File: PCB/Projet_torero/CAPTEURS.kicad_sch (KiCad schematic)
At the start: 0 parts

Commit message: kicad capteurs modif
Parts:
- added C401, C402: C_Small, symbol Device:C_Small
- added U401: ADXL343, Package_LGA:LGA-14_3x5mm_P0.8mm_LayoutBorder1x6y, symbol Sensor_Motion:ADXL343
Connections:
- new net +3.3V: C401.1, U401.3 (RES), U401.6 (Vs)
- new net +3.3VA: C402.1, U401.1 (Vdd_I/O)
- new net CS: U401.7 (~{CS})
- new net GND: C401.2, C402.2, U401.11 (RES), U401.2 (GND), U401.4 (GND), U401.5 (GND)
- new net INT1: U401.8 (INT1)
- new net INT2: U401.9 (INT2)
- new net SCLK: U401.14 (SCL/SCLK)
- new net SDA/SDI/SDIO: U401.13 (SDA/SDI/SDIO)
- new net SDO/ADDR: U401.12 (SDO/ADDR)

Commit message: modif capteurs
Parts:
- added J401: Conn_01x08, symbol Connector_Generic:Conn_01x08
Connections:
- net GND: now also J401.8 (Pin_8)
- new net +5V: J401.5 (Pin_5)
- new net DEV_EN: J401.3 (Pin_3)
- new net M_EN: J401.2 (Pin_2)
- new net M_SCTR: J401.4 (Pin_4)
- new net Rx: J401.7 (Pin_7)
- new net Tx: J401.6 (Pin_6)
- no-connect marks 0 -> 1

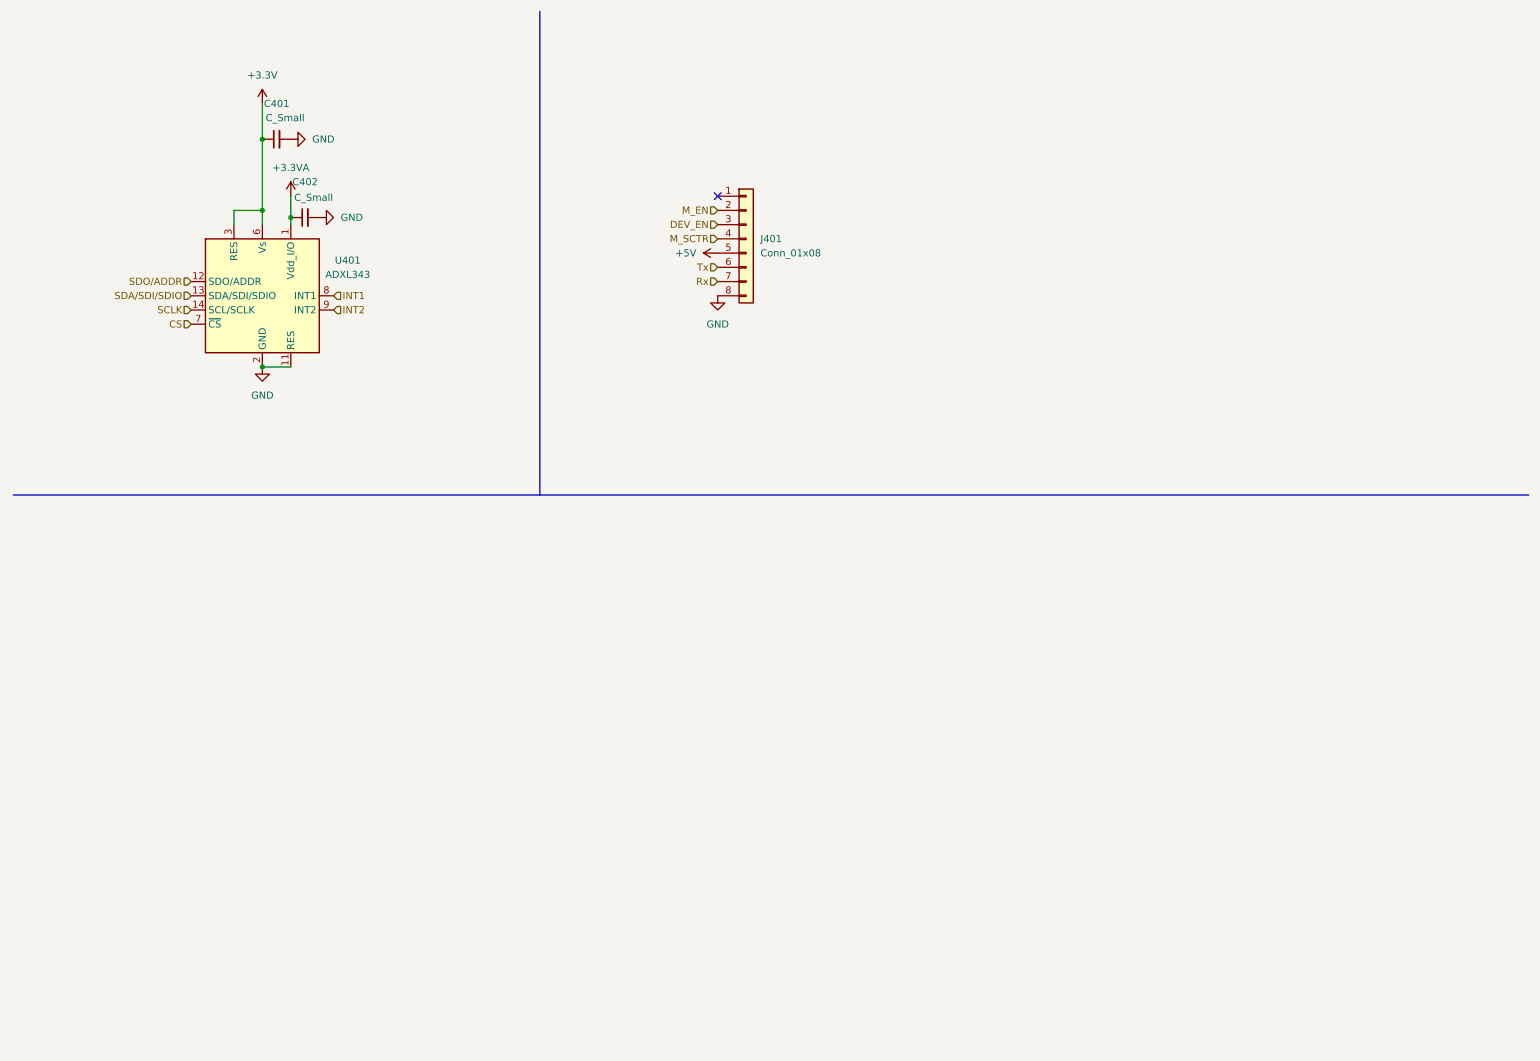
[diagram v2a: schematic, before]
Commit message: modif kicad capteur + excel liens/sources
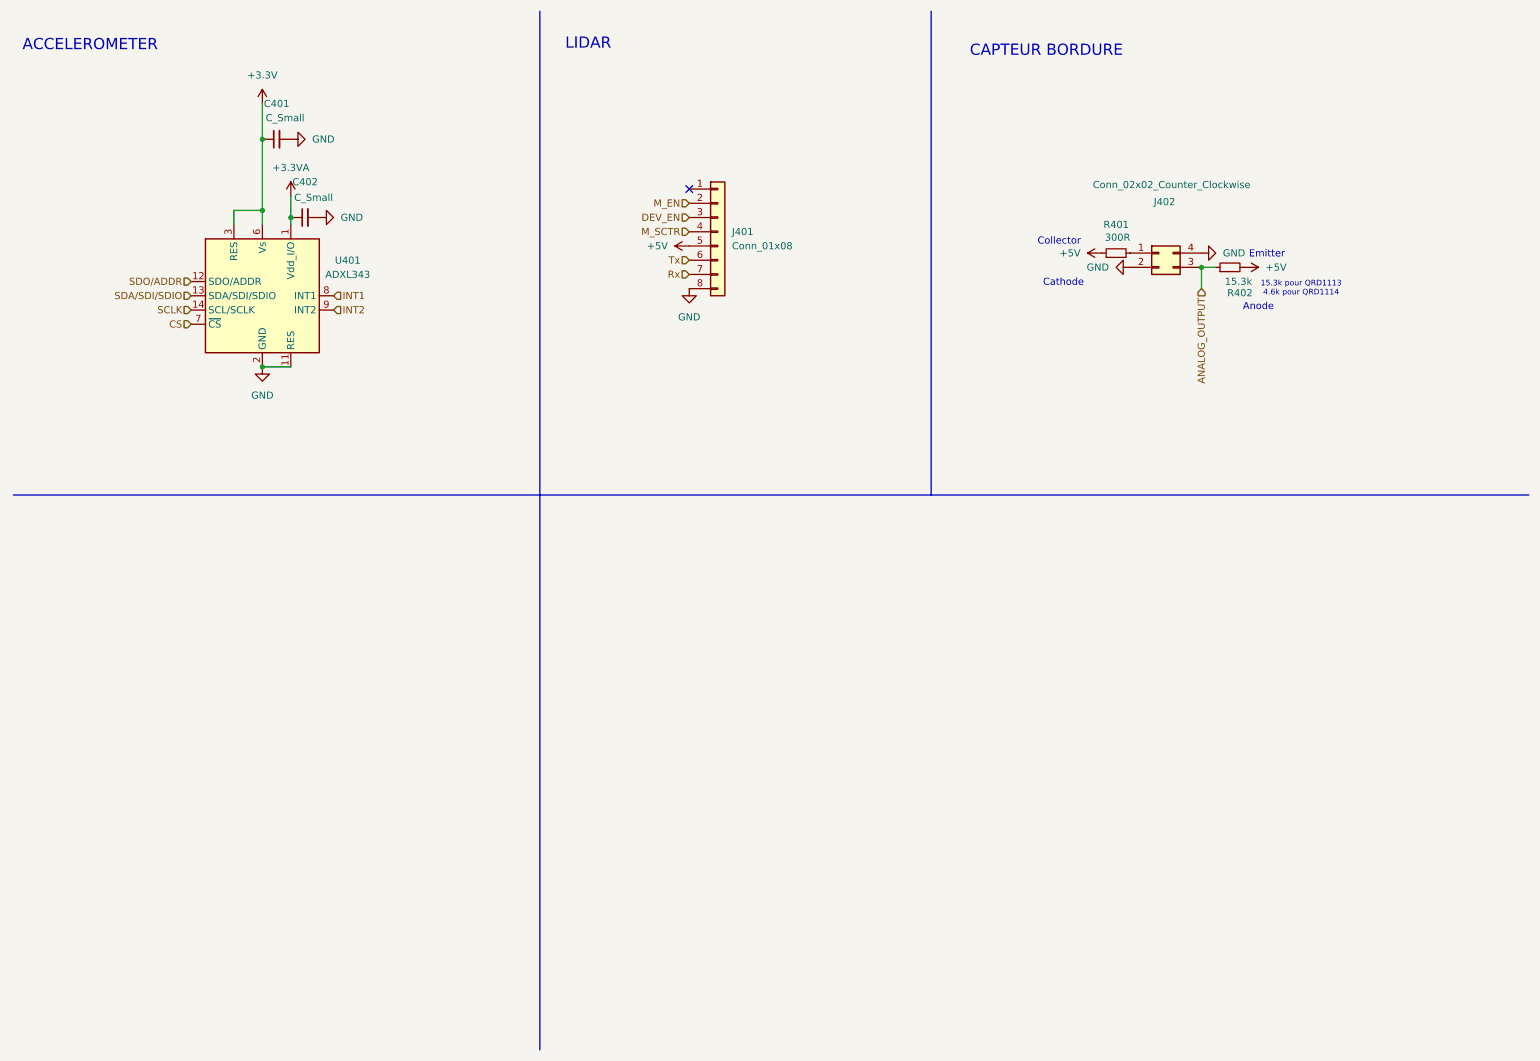
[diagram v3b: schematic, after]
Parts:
- added J402: Conn_02x02_Counter_Clockwise, symbol Connector_Generic:Conn_02x02_Counter_Clockwise
- added R401: 300R, symbol Device:R_Small
- added R402: 15.3k, symbol Device:R_Small
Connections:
- net +5V: now also R401.1, R402.2
- net GND: now also J402.2 (Pin_2), J402.4 (Pin_4)
- new net: J402.1 (Pin_1), R401.2
- new net ANALOG_OUTPUT: J402.3 (Pin_3), R402.1
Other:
- note added: "15.3k pour QRD1113 4.6k pour QRD1114"
- note added: "ACCELEROMETER"
- note added: "Anode"
- note added: "CAPTEUR BORDURE"
- note added: "Cathode"
- note added: "Collector"
- note added: "Emitter"
- note added: "LIDAR"
- moved on the sheet: J401

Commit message: modif kicad capteur
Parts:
- added J403: Conn_02x02_Counter_Clockwise, symbol Connector_Generic:Conn_02x02_Counter_Clockwise
- added R403: 300R, symbol Device:R_Small
- added R404: 15.3k, symbol Device:R_Small
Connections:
- net +5V: now also R403.1, R404.2
- net GND: now also J403.2 (Pin_2), J403.4 (Pin_4)
- net ANALOG_OUTPUT renamed ANALOG_OUTPUT_1
- new net: J403.1 (Pin_1), R403.2
- new net ANALOG_OUTPUT_2: J403.3 (Pin_3), R404.1
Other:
- moved on the sheet: J402, R401, R402

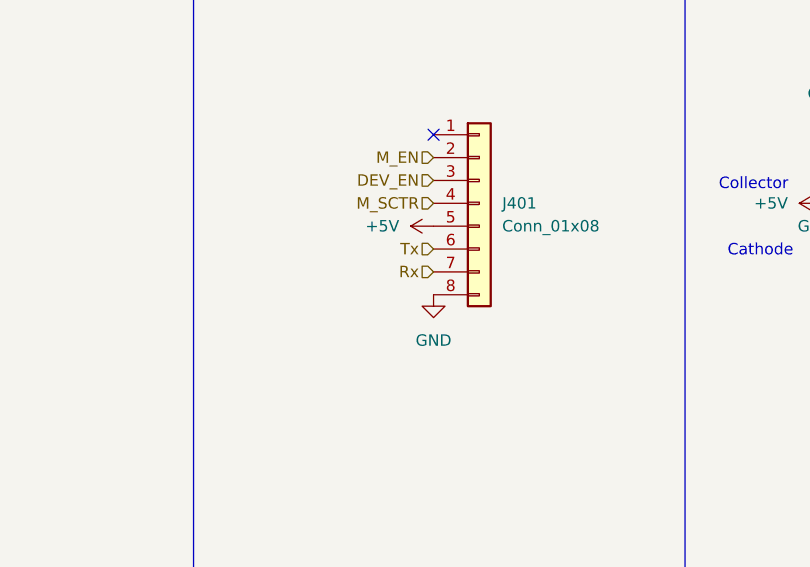
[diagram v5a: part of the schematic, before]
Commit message: Inversion pins lidar
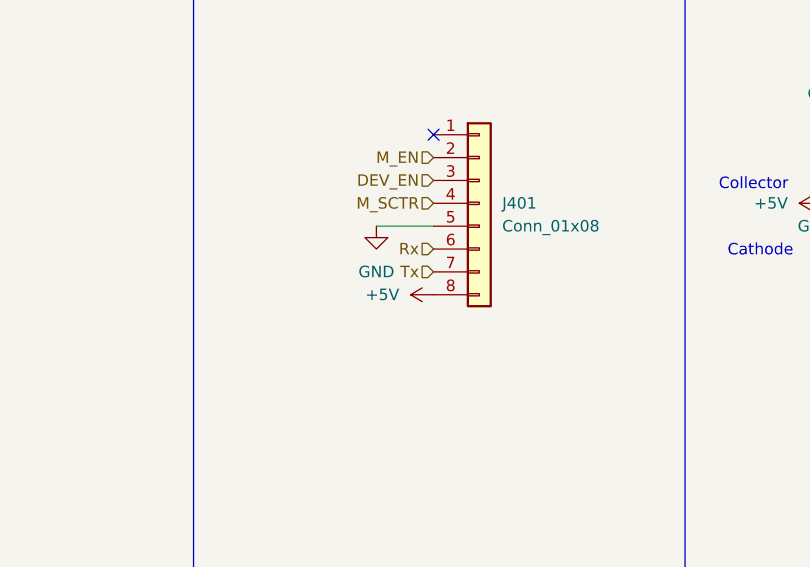
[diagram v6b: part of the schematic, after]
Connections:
- net +5V: now also J401.8 (Pin_8); no longer J401.5 (Pin_5)
- net GND: now also J401.5 (Pin_5); no longer J401.8 (Pin_8)
- net Rx: now also J401.6 (Pin_6); no longer J401.7 (Pin_7)
- net Tx: now also J401.7 (Pin_7); no longer J401.6 (Pin_6)

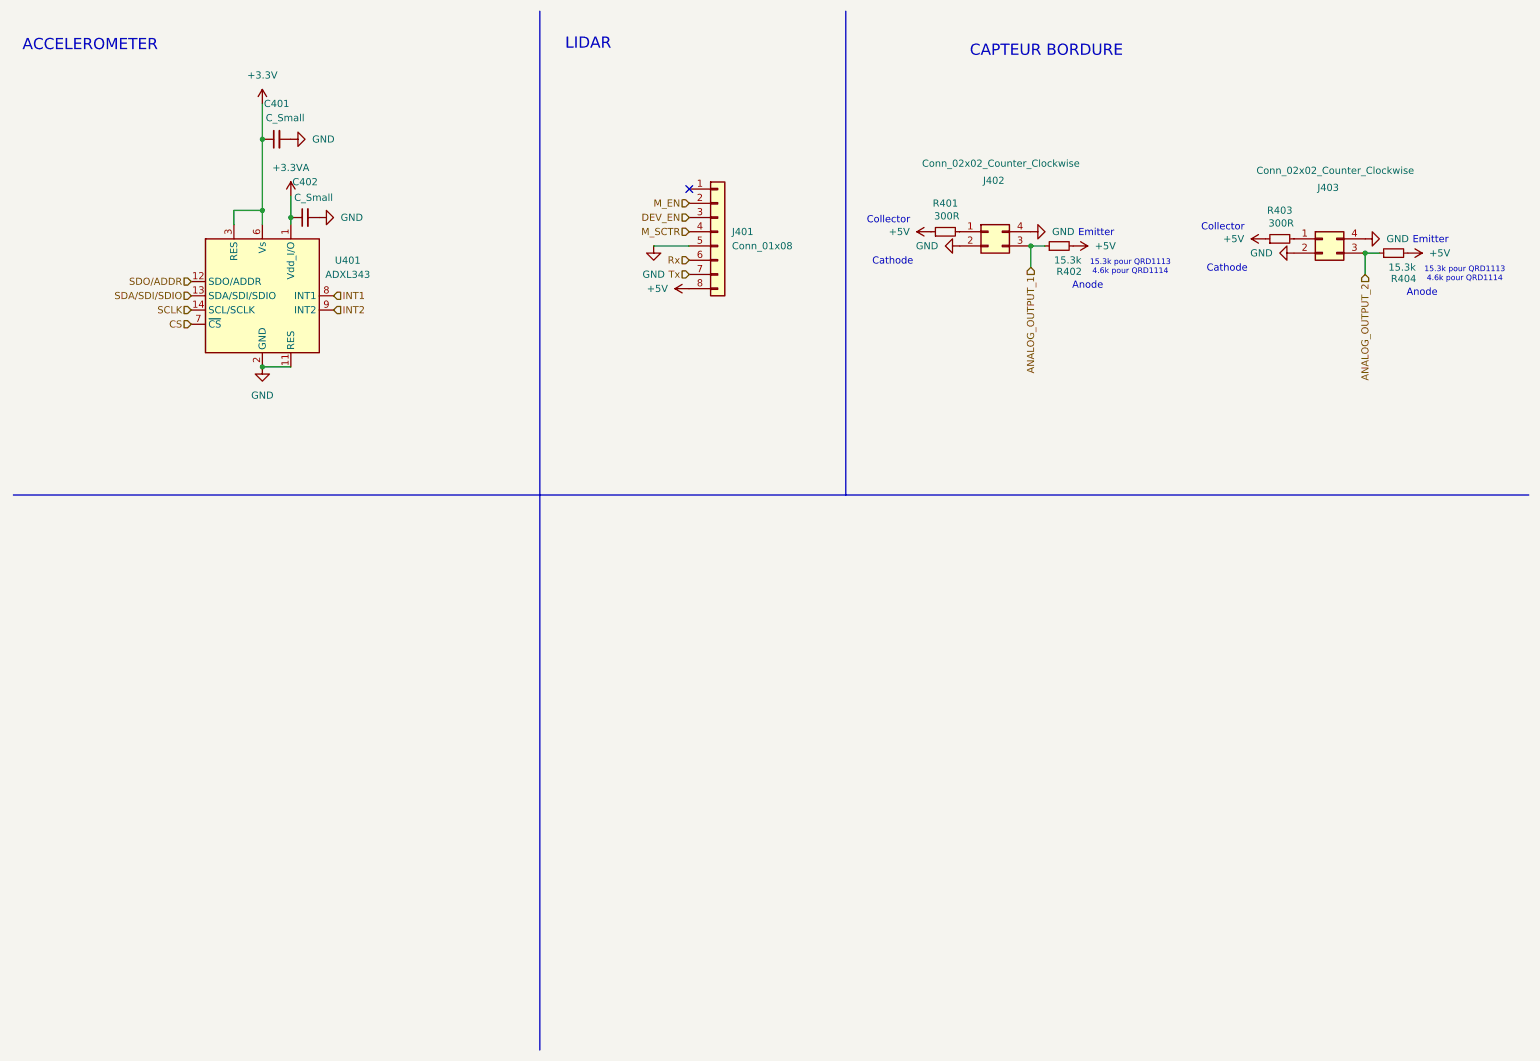
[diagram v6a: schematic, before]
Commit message: ajout nouvelles feuilles capteurs bords
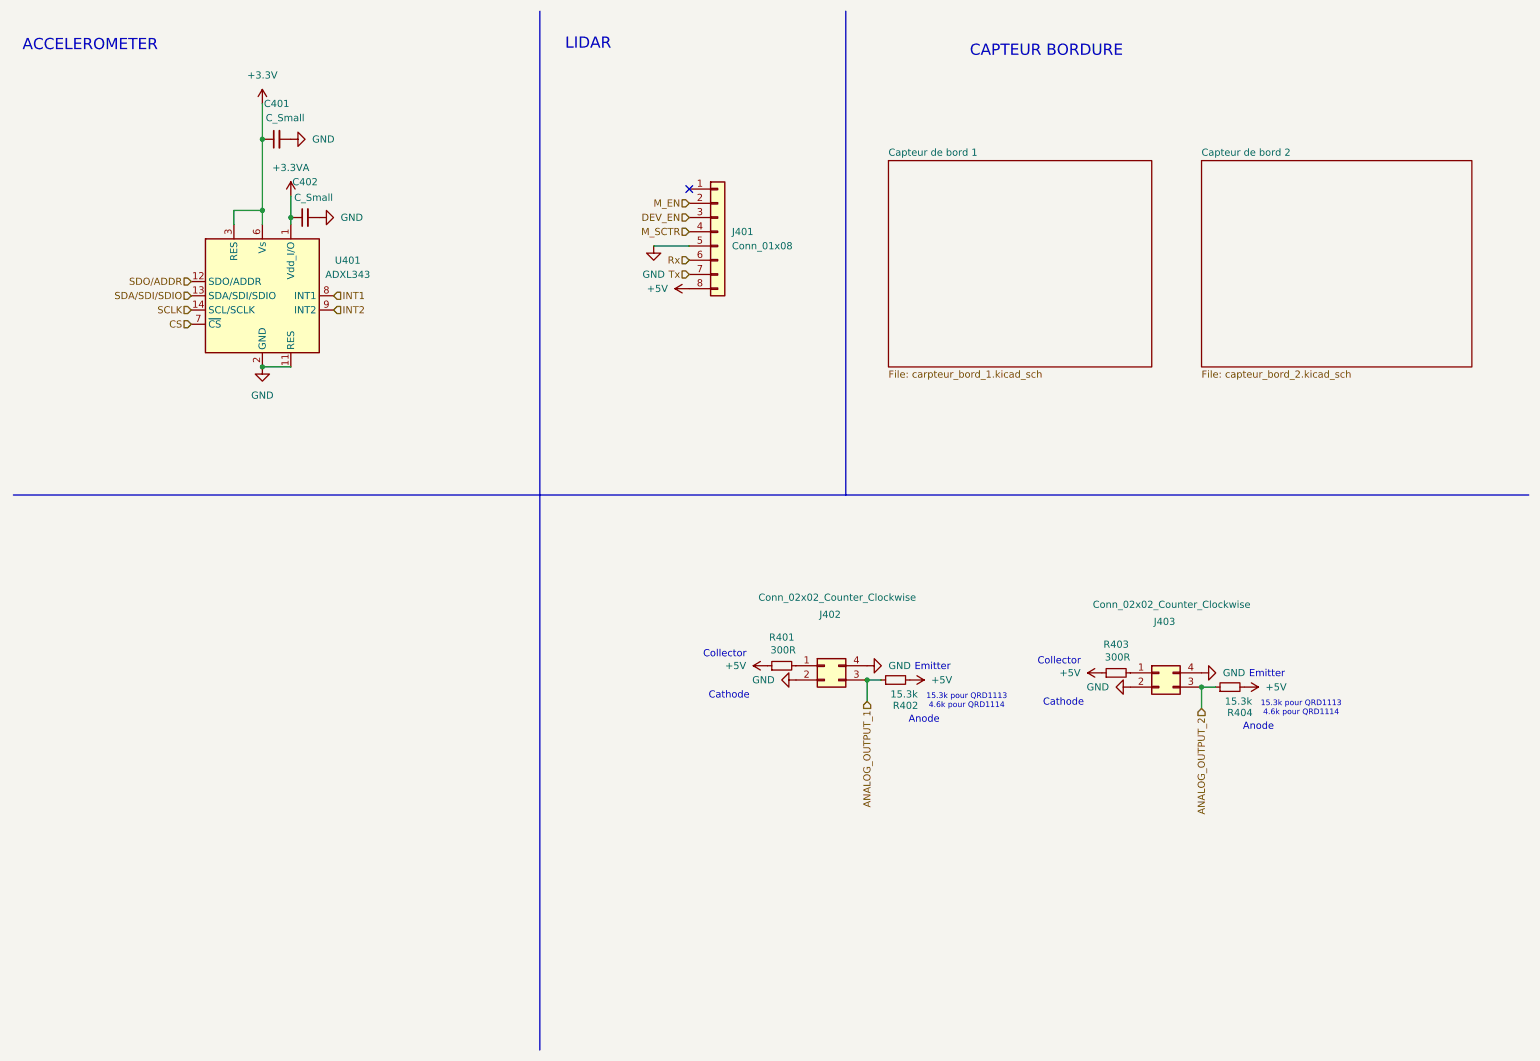
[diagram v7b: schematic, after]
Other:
- added sheet Capteur de bord 1 (carpteur_bord_1.kicad_sch)
- added sheet Capteur de bord 2 (capteur_bord_2.kicad_sch)
- moved on the sheet: J402, J403, R401, R402, R403, R404

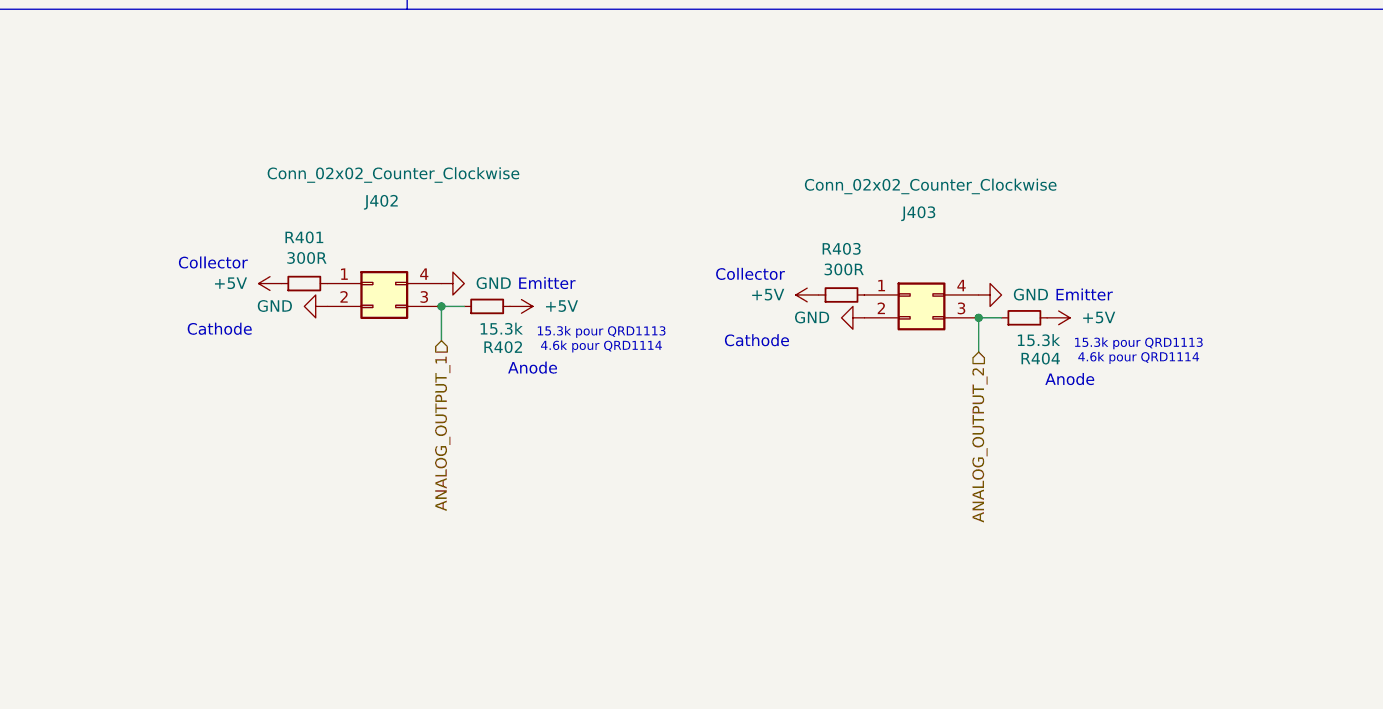
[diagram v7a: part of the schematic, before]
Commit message: ajout modif capteurs de bord
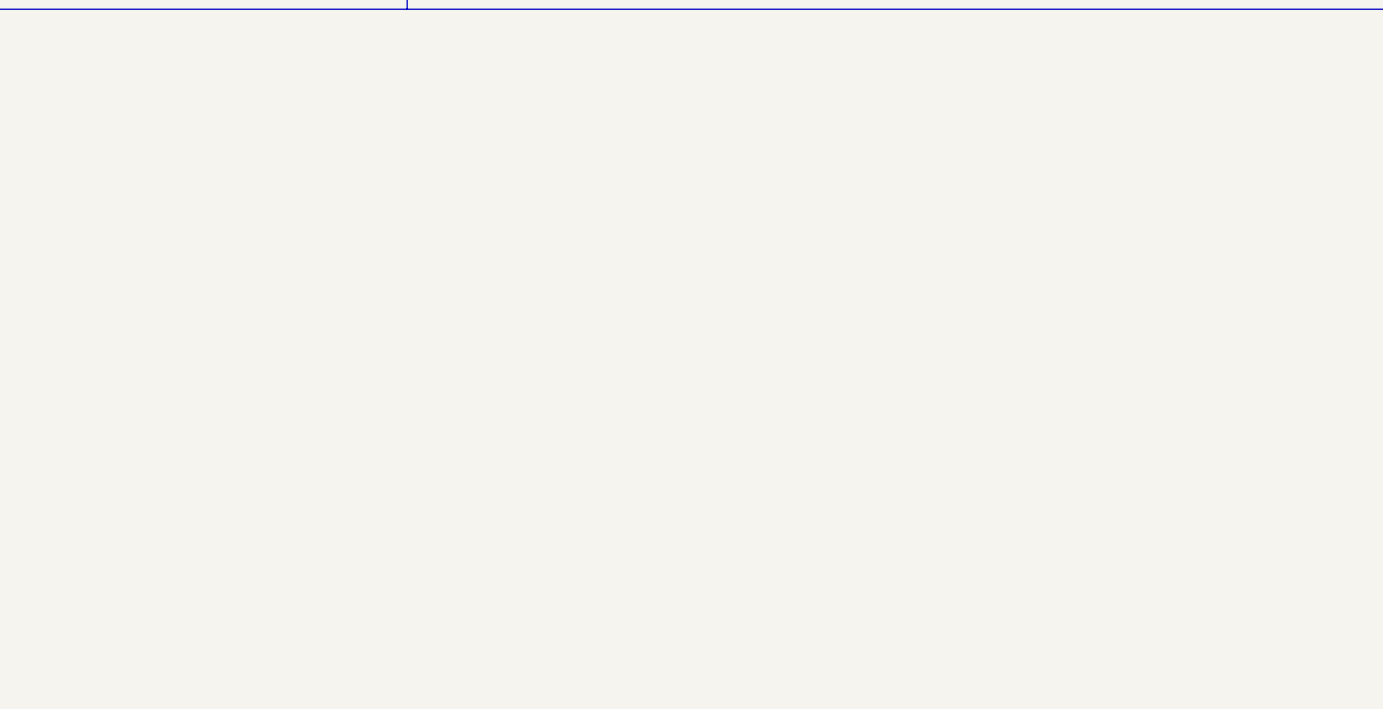
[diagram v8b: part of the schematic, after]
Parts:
- removed J402, J403: Conn_02x02_Counter_Clockwise, symbol Connector_Generic:Conn_02x02_Counter_Clockwise
- removed R401, R403: 300R, symbol Device:R_Small
- removed R402, R404: 15.3k, symbol Device:R_Small
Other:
- note removed: "15.3k pour QRD1113 4.6k pour QRD1114"
- note removed: "Anode"
- note removed: "Cathode"
- note removed: "Collector"
- note removed: "Emitter"
